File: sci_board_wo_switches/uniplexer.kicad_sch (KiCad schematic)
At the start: 4 parts, among them U7 TCA9546APWR

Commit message: EPS AVI SCI SCIwoSwitches RF AUX all updated to use RNs. BOMs completed
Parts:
- C67: MANUFACTURER Murata -> (none); Manufacturer (none) -> Murata; PARTREV GRM188R61E106KA73D -> (none); Part Number (none) -> GRM188R61E106KA73D
- C68: MANUFACTURER Murata -> (none); Manufacturer (none) -> Murata; PARTREV GRM155R61E104KA87D -> (none); Part Number (none) -> GRM155R61E104KA87D
- R39: Manufacturer (none) -> YAGEO; Part Number (none) -> RC0402FR-07100KL; Tolerance (none) -> 1
- U7: Manufacturer (none) -> TI; Part Number (none) -> TCA9546APWR
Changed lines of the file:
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@@
-			)
-		)
-		(property "MANUFACTURER" "Murata"
-			(at 118.745 123.825 0)
-			(effects
-				(font
-					(size 1.27 1.27)
-				)
-				(hide yes)
-			)
-		)
-		(property "MAXIMUM_PACKAGE_HEIGHT" ""
-			(at 118.745 123.825 0)
-			(effects
-				(font
-					(size 1.27 1.27)
-				)
-				(hide yes)
-			)
-		)
-		(property "PARTREV" "GRM188R61E106KA73D"
-			(at 118.745 123.825 0)
-			(effects
-				(font
-					(size 1.27 1.27)
-				)
-				(hide yes)
-			)
-		)
-		(property "STANDARD" ""
-			(at 118.745 123.825 0)
-			(effects
-				(font
-					(size 1.27 1.27)
-				)
-				(hide yes)
 			)
 		)
@@
 		)
 		(property "Temperture Coefficient" "X5R"
+			(at 118.745 123.825 0)
+			(effects
+				(font
+					(size 1.27 1.27)
+				)
+				(hide yes)
+			)
+		)
+		(property "Manufacturer" "Murata"
+			(at 118.745 123.825 0)
+			(effects
+				(font
+					(size 1.27 1.27)
+				)
+				(hide yes)
+			)
+		)
+		(property "Part Number" "GRM188R61E106KA73D"
 			(at 118.745 123.825 0)
 			(effects
@@
 			)
 		)
+		(property "Manufacturer" "TI"
+			(at 40.005 117.475 0)
+			(effects
+				(font
+					(size 1.27 1.27)
+				)
+				(hide yes)
+			)
+		)
+		(property "Part Number" "TCA9546APWR"
+			(at 40.005 117.475 0)
+			(effects
+				(font
+					(size 1.27 1.27)
+				)
+				(hide yes)
+			)
+		)
 		(pin "11"
 		)
@@
 			)
 		)
-		(property "Datasheet" "~"
+		(property "Datasheet" "https://www.yageo.com/upload/media/product/app/datasheet/rchip/pyu-rt_1-to-0.01_rohs_l.pdf"
 			(at 19.685 128.27 0)
 			(effects
@@
 		)
 		(property "Description" "Resistor"
+			(at 19.685 128.27 0)
+			(effects
+				(font
+					(size 1.27 1.27)
+				)
+				(hide yes)
+			)
+		)
+		(property "Manufacturer" "YAGEO"
+			(at 19.685 128.27 0)
+			(effects
+				(font
+					(size 1.27 1.27)
+				)
+				(hide yes)
+			)
+		)
+		(property "Part Number" "RC0402FR-07100KL"
+			(at 19.685 128.27 0)
+			(effects
+				(font
+					(size 1.27 1.27)
+				)
+				(hide yes)
+			)
+		)
+		(property "Tolerance" "1"
 			(at 19.685 128.27 0)
 			(effects
@@
 			)
 		)
-		(property "MANUFACTURER" "Murata"
-			(at 128.27 123.825 0)
-			(effects
-				(font
-					(size 1.27 1.27)
-				)
-				(hide yes)
-			)
-		)
-		(property "MAXIMUM_PACKAGE_HEIGHT" ""
-			(at 128.27 123.825 0)
-			(effects
-				(font
-					(size 1.27 1.27)
-				)
-				(hide yes)
-			)
-		)
-		(property "PARTREV" "GRM155R61E104KA87D"
-			(at 128.27 123.825 0)
-			(effects
-				(font
-					(size 1.27 1.27)
-				)
-				(hide yes)
-			)
-		)
-		(property "STANDARD" ""
-			(at 128.27 123.825 0)
-			(effects
-				(font
-					(size 1.27 1.27)
-				)
-				(hide yes)
-			)
-		)
 		(property "Color" ""
 			(at 128.27 123.825 0)
@@
 			(at 128.27 123.825 0)
 			(effects
+				(font
+					(size 1.27 1.27)
+				)
+				(hide yes)
+			)
+		)
+		(property "Manufacturer" "Murata"
+			(at 128.27 123.825 0)
+			(effects
+				(font
+					(size 1.27 1.27)
+				)
+				(hide yes)
+			)
+		)
+		(property "Part Number" "GRM155R61E104KA87D"
+			(at 128.27 123.825 0)
+			(effects

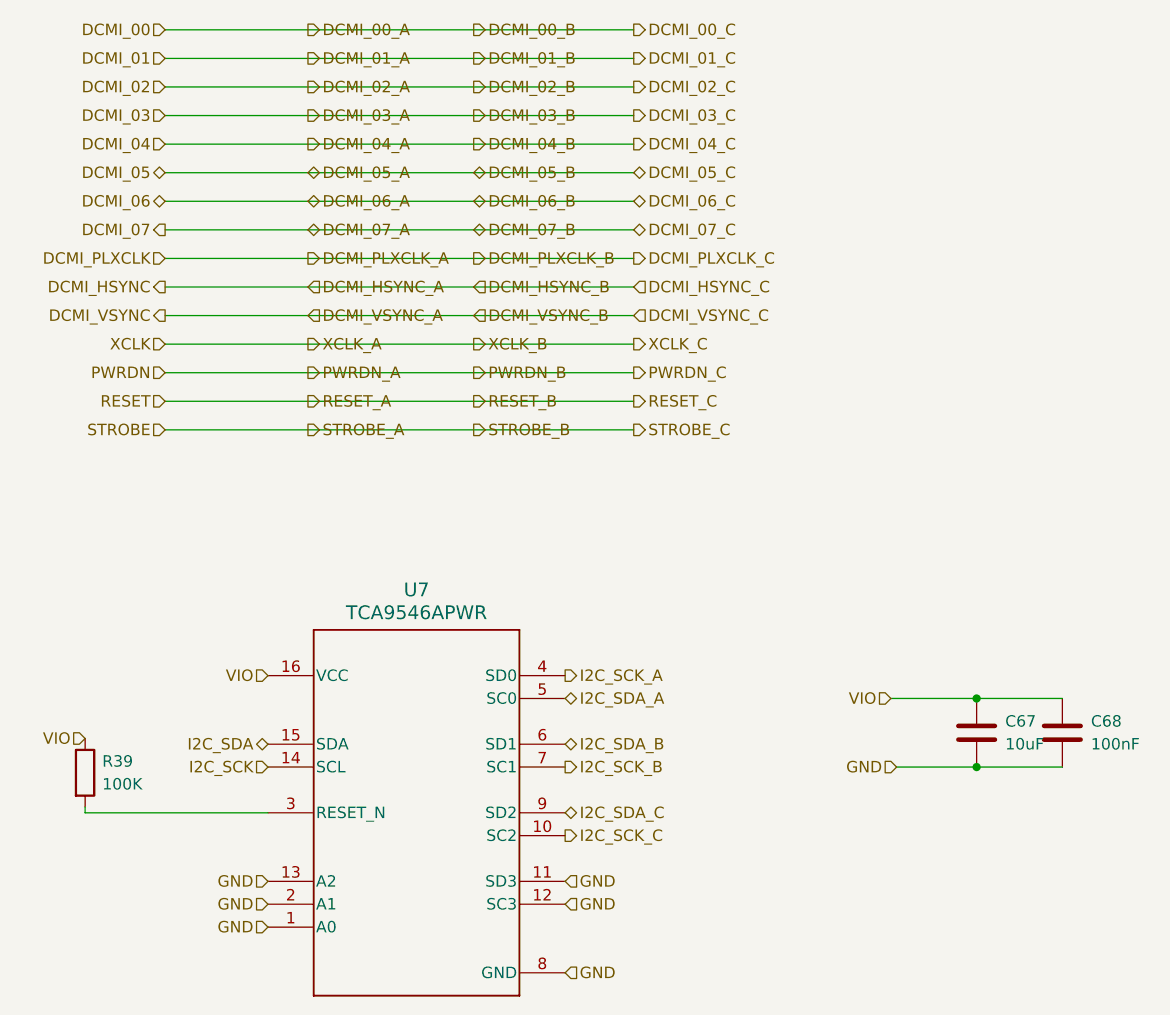
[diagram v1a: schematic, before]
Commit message: sorting out pullups on resets and attention. replace reset with RN where possible. Introduce CN to save some parts
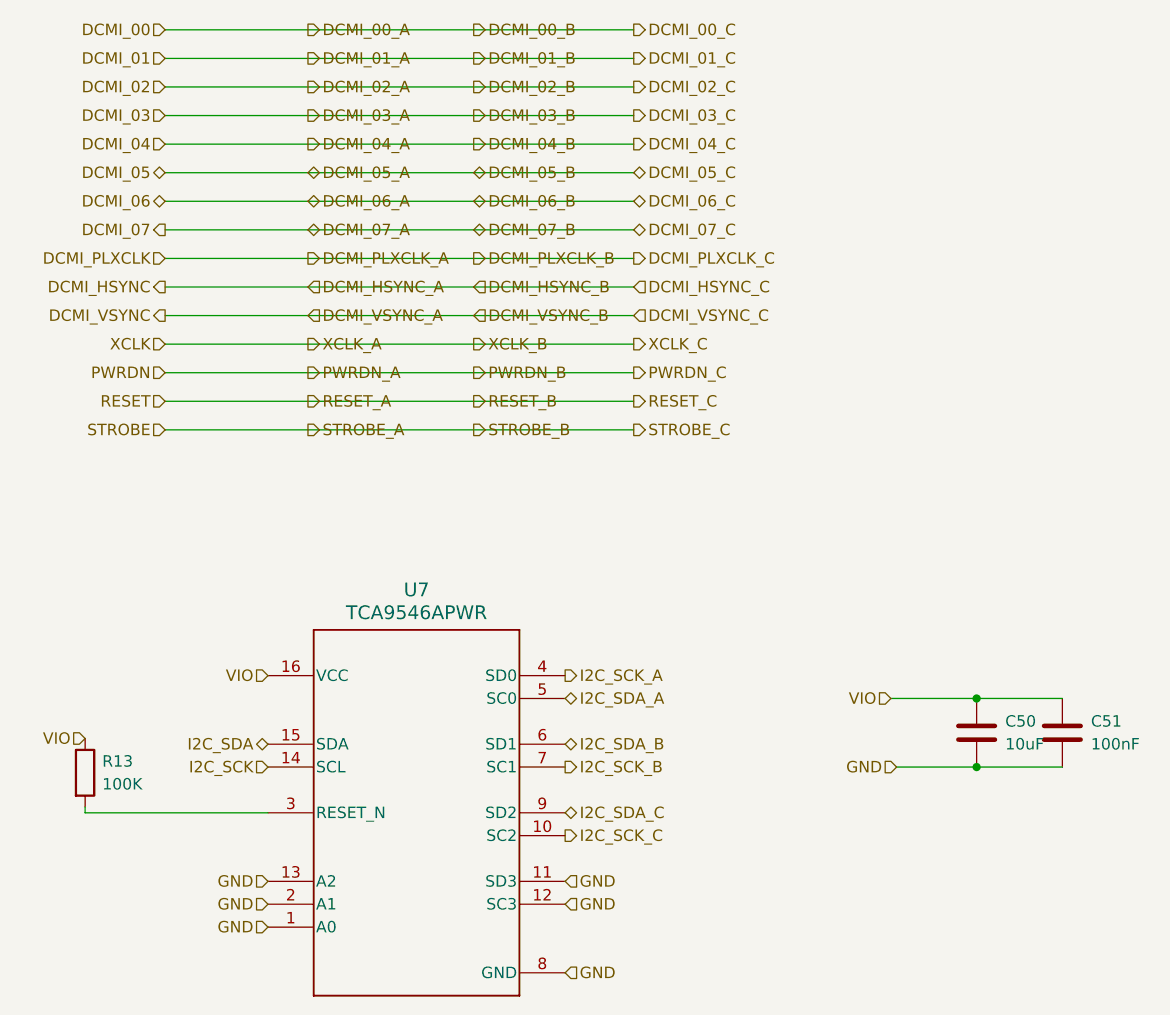
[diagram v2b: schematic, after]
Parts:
- renumbered C67 to C50, C68 to C51, R39 to R13
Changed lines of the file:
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@@
 		(dnp no)
 		(fields_autoplaced yes)
-		(property "Reference" "C67"
+		(property "Reference" "C50"
 			(at 121.92 122.5549 0)
 			(effects
@@
 			(project "sci_board_wo_switches"
 				(path "/b4b2c88d-f6cd-4e60-862d-e21f68728580/5e5b27f8-7a4c-45d0-95f8-aff71797fcd3/9605d53d-4070-4037-ab55-0e19ed326c8d"
-					(reference "C67")
+					(reference "C50")
 					(unit 1)
 				)
@@
 				(font
 					(size 1.27 1.27)
-					(italic yes)
 				)
 				(hide yes)
@@
 				(font
 					(size 1.27 1.27)
-					(italic yes)
 				)
 				(hide yes)
@@
 		(dnp no)
 		(fields_autoplaced yes)
-		(property "Reference" "R39"
+		(property "Reference" "R13"
 			(at 21.59 126.9999 0)
 			(effects
@@
 			(project ""
 				(path "/b4b2c88d-f6cd-4e60-862d-e21f68728580/5e5b27f8-7a4c-45d0-95f8-aff71797fcd3/9605d53d-4070-4037-ab55-0e19ed326c8d"
-					(reference "R39")
+					(reference "R13")
 					(unit 1)
 				)
@@
 		(dnp no)
 		(fields_autoplaced yes)
-		(property "Reference" "C68"
+		(property "Reference" "C51"
 			(at 131.445 122.5549 0)
 			(effects
@@
 			(project "sci_board_wo_switches"
 				(path "/b4b2c88d-f6cd-4e60-862d-e21f68728580/5e5b27f8-7a4c-45d0-95f8-aff71797fcd3/9605d53d-4070-4037-ab55-0e19ed326c8d"
-					(reference "C68")
+					(reference "C51")
 					(unit 1)
 				)

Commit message: checked BOM for sci wo switches
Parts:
- renumbered R13 to R11
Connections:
- net I2C_RST: now reaches R11.2, U7.3 (RESET_N)
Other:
- moved on the sheet: R11
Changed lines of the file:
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@@
 	(wire
 		(pts
-			(xy 19.685 132.08) (xy 19.685 132.715)
+			(xy 24.13 132.08) (xy 24.13 132.715)
 		)
 		(stroke
@@
 	(wire
 		(pts
-			(xy 40.005 132.715) (xy 19.685 132.715)
+			(xy 40.005 132.715) (xy 24.13 132.715)
 		)
 		(stroke
@@
 	(hierarchical_label "VIO"
 		(shape input)
-		(at 19.685 124.46 180)
+		(at 24.13 124.46 180)
 		(effects
 			(font
@@
 		(shape input)
 		(at 40.005 142.875 180)
+		(effects
+			(font
+				(size 1.27 1.27)
+			)
+			(justify right)
+		)
+	)
+	(hierarchical_label "I2C_RST"
+		(shape input)
+		(at 24.13 132.715 180)
 		(effects
 			(font
@@
 			)
 		)
-		(property "Description" ""
+		(property "Description" "IC BUS SWITCH 2 X 1:4 16-TSSOP"
 			(at 40.005 117.475 0)
 			(effects
@@
 	(symbol
 		(lib_id "Device:R")
-		(at 19.685 128.27 0)
+		(at 24.13 128.27 0)
 		(unit 1)
 		(exclude_from_sim no)
@@
 		(dnp no)
 		(fields_autoplaced yes)
-		(property "Reference" "R13"
-			(at 21.59 126.9999 0)
+		(property "Reference" "R11"
+			(at 26.035 126.9999 0)
 			(effects
 				(font
@@
 		)
 		(property "Value" "100K"
-			(at 21.59 129.5399 0)
+			(at 26.035 129.5399 0)
 			(effects
 				(font
@@
 		)
 		(property "Footprint" "Resistor_SMD:R_0402_1005Metric_Pad0.72x0.64mm_HandSolder"
-			(at 17.907 128.27 90)
-			(effects
-				(font
-					(size 1.27 1.27)
-				)
-				(hide yes)
-			)
-		)
-		(property "Datasheet" "https://www.yageo.com/upload/media/product/app/datasheet/rchip/pyu-rt_1-to-0.01_rohs_l.pdf"
-			(at 19.685 128.27 0)
+			(at 22.352 128.27 90)
+			(effects
+				(font
+					(size 1.27 1.27)
+				)
+				(hide yes)
+			)
+		)
+		(property "Datasheet" "https://www.yageo.com/upload/media/product/products/datasheet/rchip/PYu-RC_Group_51_RoHS_L_12.pdf"
+			(at 24.13 128.27 0)
 			(effects
 				(font
@@
 		)
 		(property "Description" "Resistor"
-			(at 19.685 128.27 0)
+			(at 24.13 128.27 0)
 			(effects
 				(font
@@
 		)
 		(property "Manufacturer" "YAGEO"
-			(at 19.685 128.27 0)
+			(at 24.13 128.27 0)
 			(effects
 				(font
@@
 		)
 		(property "Part Number" "RC0402FR-07100KL"
-			(at 19.685 128.27 0)
+			(at 24.13 128.27 0)
 			(effects
 				(font
@@
 		)
 		(property "Tolerance" "1"
-			(at 19.685 128.27 0)
+			(at 24.13 128.27 0)
 			(effects
 				(font
@@
 			(project ""
 				(path "/b4b2c88d-f6cd-4e60-862d-e21f68728580/5e5b27f8-7a4c-45d0-95f8-aff71797fcd3/9605d53d-4070-4037-ab55-0e19ed326c8d"
-					(reference "R13")
+					(reference "R11")
 					(unit 1)
 				)

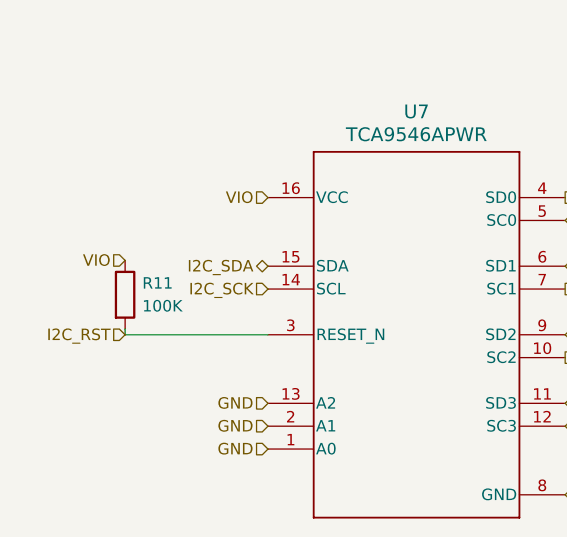
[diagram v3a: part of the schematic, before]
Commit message: move SPI CS pullups to outer schema to combine multiple with RNs
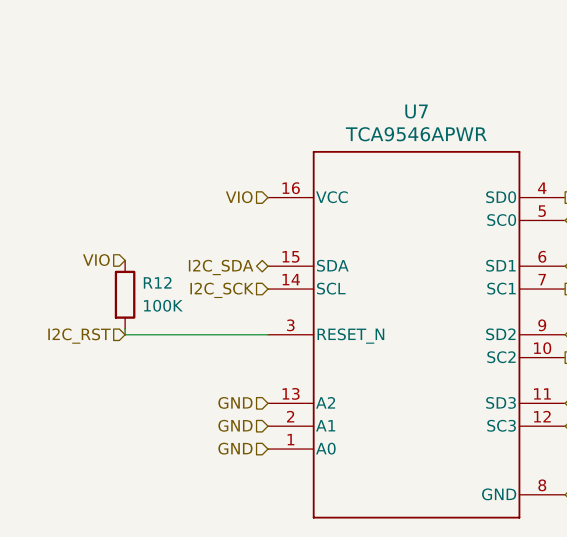
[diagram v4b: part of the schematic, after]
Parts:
- renumbered R11 to R12
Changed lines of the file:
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@@
 		(dnp no)
 		(fields_autoplaced yes)
-		(property "Reference" "R11"
+		(property "Reference" "R12"
 			(at 26.035 126.9999 0)
 			(effects
@@
 			(project ""
 				(path "/b4b2c88d-f6cd-4e60-862d-e21f68728580/5e5b27f8-7a4c-45d0-95f8-aff71797fcd3/9605d53d-4070-4037-ab55-0e19ed326c8d"
-					(reference "R11")
+					(reference "R12")
 					(unit 1)
 				)

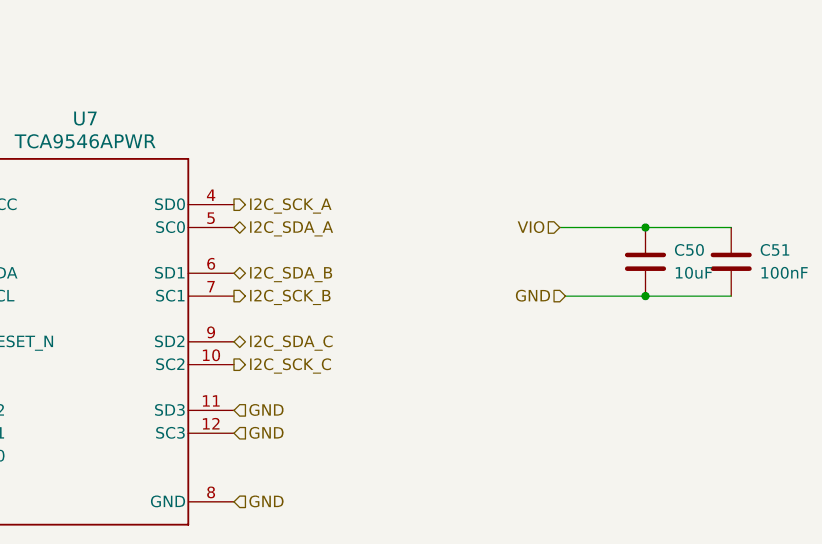
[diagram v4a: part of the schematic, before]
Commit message: SCI bodge board to correct I2C switching
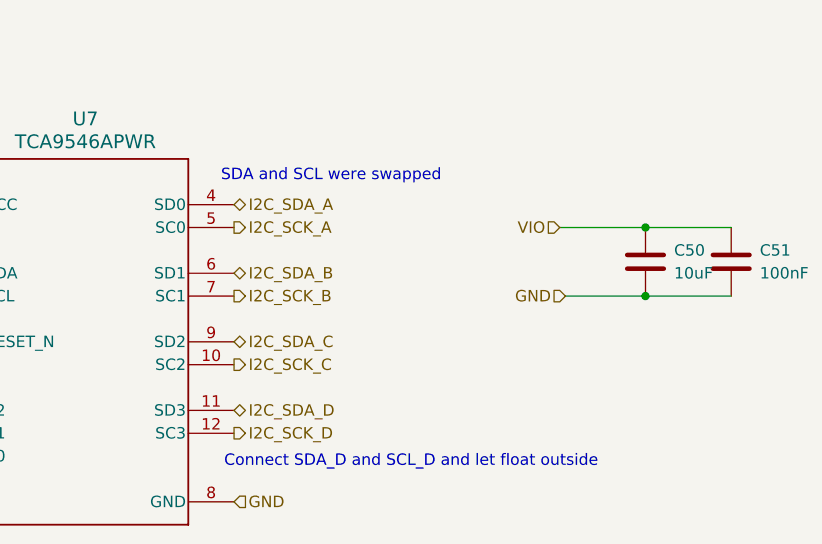
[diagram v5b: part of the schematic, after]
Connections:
- net GND: no longer U7.11 (SD3), U7.12 (SC3)
- net I2C_SCK_A: now also U7.5 (SC0); no longer U7.4 (SD0)
- net I2C_SDA_A: now also U7.4 (SD0); no longer U7.5 (SC0)
- new net I2C_SCK_D: U7.12 (SC3)
- new net I2C_SDA_D: U7.11 (SD3)
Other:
- note added: "Connect SDA_D and SCL_D and let float outside"
- note added: "SDA and SCL were swapped"
